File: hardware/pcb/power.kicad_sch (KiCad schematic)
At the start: 53 parts, among them J1 XT30PW-F, J12 Solar, J13 USB-C, U1 AP63205, U11 USBLC6, U12 TP5100, U7 CN3722, U8 MT3608

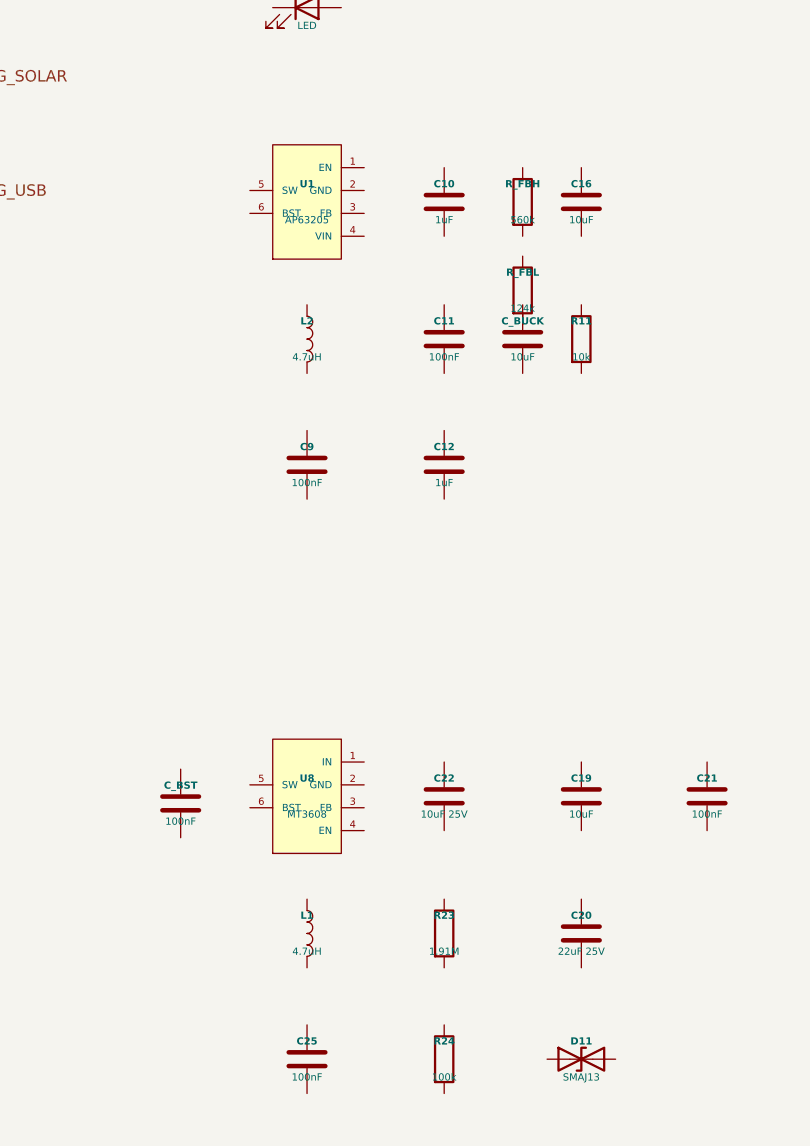
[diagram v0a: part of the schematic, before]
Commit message: hw(pcb): electrical review pass — fix 3V3 regulator variant, boost topology, GPIO13 LED conflict
Full electrical-correctness-gate review of the fresh-start design. Two of
the four CRITICALs from the 2026-05-25 senior review were resolved
incorrectly; this pass corrects them and fixes new findings:

- U1: AP63205WU is the 5 V fixed variant and the R_FBH/R_FBL values
  (560k/124k) assume a 0.6 V reference no AP6320x has — every
  combination overdrives the 3V3 rail. Swap to AP63203WU (3.3 V fixed),
  FB tied to +3V3, R_FBH/R_FBL marked DNP.
- MT3608B VLOOP: documented wiring was a buck topology and the BOM had
  no output rectifier (async boost cannot work without one). Corrected
  to VBAT→L1→SW, added D15 (SS34) and a Q3/Q4 load-disconnect so VBAT
  doesn't leak to the loop terminals through L1+D15 during deep sleep.
- Status LED moved GPIO13 → GPIO14: a green LED + 1k on GPIO13 holds
  the factory-reset strap LOW at boot → NVS wipe every boot. TP13 pad
  added for field factory reset.
- Battery divider reworked to high-side P-FET (Q5): the low-side switch
  left AIN2 biased above ADS1115 VDD through R7 (~14 uA sleep leak).
  C8 100nF → 1nF to fit the firmware's 1 ms enable window.
- TVS D8/D14 SMAJ28CA → SMAJ24CA (zero margin to CN3722 28 V abs max);
  C17 → 35 V/1206; C21 → 50 V; D6 footprint SOD-123 → SMB.
- /CHRG_SOLAR pull-up (R25), VBOOST_EN pull-down (R27), ESP32 EN RC
  (R15/C36) added; C25 duplicate bootstrap cap deleted; C16 assigned as
  U1 VIN bulk.
- schematic_connections.md rewritten pin-name-based with a symbol
  pin-number verification table and datasheet-verification blocker list;
  BOM/placement/guide/placement-script reconciled (phantom refdes,
  wrong ADS1115 pin numbers, mis-documented MPPT divider, shunt return
  path contradiction).

Flagged, not fixed: TP5100 cannot charge 2S from 5 V USB (step-down
charger) — needs an IC swap; schematic still has zero drawn wires; five
IC symbol pinouts pending datasheet verification before ordering.

Co-Auth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
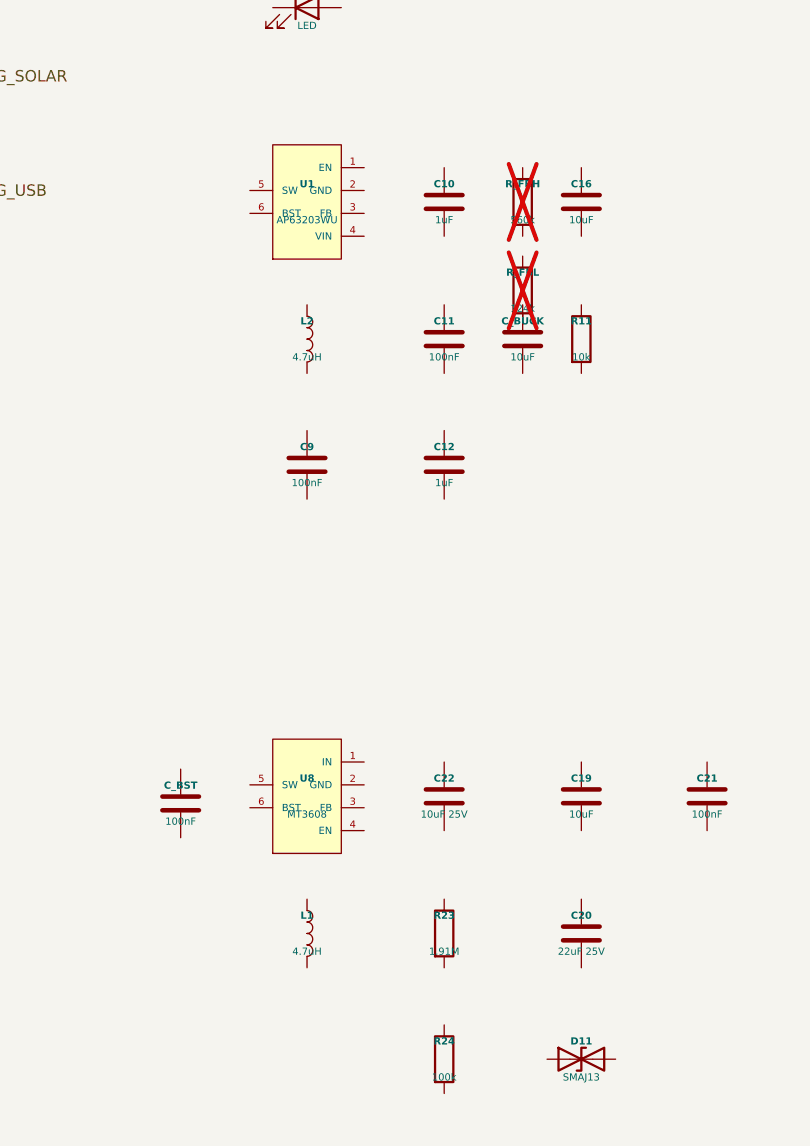
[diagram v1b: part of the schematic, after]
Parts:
- removed C25: 100nF, Capacitor_SMD:C_0402_1005Metric, symbol Device:C
- R_FBH, R_FBL: now not fitted
- U1: value AP63205 -> AP63203WU
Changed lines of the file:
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@@
 	(symbol
 		(lib_id "Device:C")
-		(at 66.04 185.42 0)
-		(unit 1)
-		(body_style 1)
-		(exclude_from_sim no)
-		(in_bom yes)
-		(on_board yes)
-		(in_pos_files yes)
-		(dnp no)
-		(fields_autoplaced yes)
-		(property "Reference" "C25"
-			(at 66.04 183.42 0)
-			(show_name no)
-			(do_not_autoplace no)
-			(effects
-				(font
-					(size 0.8 0.8)
-					(bold yes)
-				)
-			)
-		)
-		(property "Value" "100nF"
-			(at 66.04 187.42 0)
-			(show_name no)
-			(do_not_autoplace no)
-			(effects
-				(font
-					(size 0.8 0.8)
-				)
-			)
-		)
-		(property "Footprint" "Capacitor_SMD:C_0402_1005Metric"
-			(at 0 0 0)
-			(hide yes)
-			(show_name no)
-			(do_not_autoplace no)
-			(effects
-				(font
-					(size 0.8 0.8)
-				)
-			)
-		)
-		(property "Datasheet" ""
-			(at 0 0 0)
-			(hide yes)
-			(show_name no)
-			(do_not_autoplace no)
-			(effects
-				(font
-					(size 0.8 0.8)
-				)
-			)
-		)
-		(property "Description" ""
-			(at 0 0 0)
-			(hide yes)
-			(show_name no)
-			(do_not_autoplace no)
-			(effects
-				(font
-					(size 0.8 0.8)
-				)
-			)
-		)
-		(property "LCSC" "C14663"
-			(at 0 0 0)
-			(hide yes)
-			(show_name no)
-			(do_not_autoplace no)
-			(effects
-				(font
-					(size 0.8 0.8)
-				)
-			)
-		)
-		(pin "1"
-		)
-		(pin "2"
-		)
-		(instances
-			(project "welld"
-				(path "/58c9365f-ec30-52a7-98fc-0e15b15bee29"
-					(reference "C25")
-					(unit 1)
-				)
-				(path "/58c9365f-ec30-52a7-98fc-0e15b15bee29/64fba67a-e021-5c3c-b6fb-14c5c55ee35f/0ab162ba-e49c-5e89-8571-5a4794668fb8"
-					(reference "C25")
-					(unit 1)
-				)
-			)
-		)
-	)
-	(symbol
-		(lib_id "Device:C")
 		(at 185.42 39.37 0)
 		(unit 1)
@@
 			)
 		)
-		(property "Value" "AP63205"
+		(property "Value" "AP63203WU"
 			(at 66.04 92.17 0)
 			(show_name no)
@@
 		(on_board yes)
 		(in_pos_files yes)
-		(dnp no)
+		(dnp yes)
 		(fields_autoplaced yes)
 		(property "Reference" "R_FBH"
@@
 		(on_board yes)
 		(in_pos_files yes)
-		(dnp no)
+		(dnp yes)
 		(fields_autoplaced yes)
 		(property "Reference" "R_FBL"

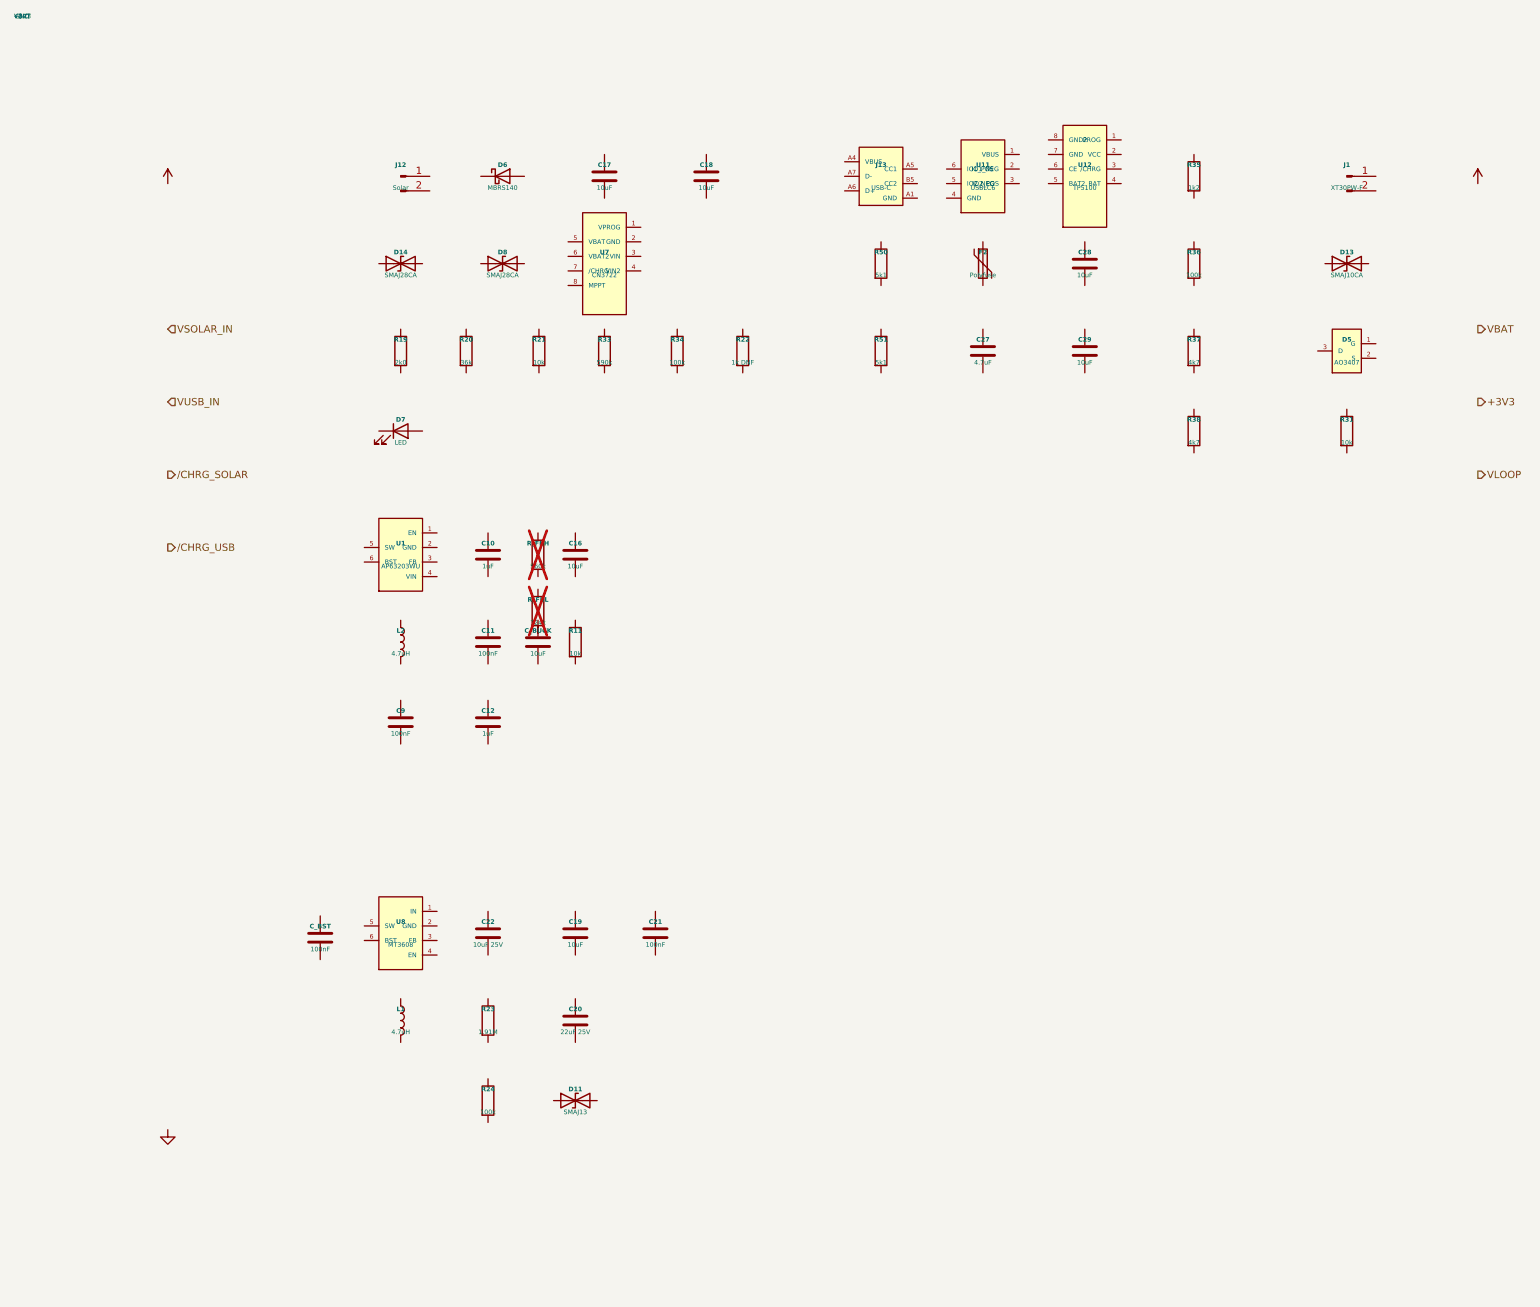
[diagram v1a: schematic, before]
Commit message: hw(pcb): symbol pass — all parts placed, CN3722 redrawn TSSOP-16, CV/MPPT reference bug fixed
Clears the layout gate from senior_review_2026-07-06.md (CRITICALs 1-3)
and fixes a newly found CRITICAL:

- CN3722 CV divider was computed with the CN3791's 1.205 V reference;
  the CN3722's FB reference is 2.416 V (datasheet Rev 1.1, p.4), so the
  documented 590k/100k divider would regulate the 2S pack at ~16.7 V.
  R33 590k -> 243k (8.287 V; formula V_REG = 2.416 x (1 + Rh/Rl) stated
  at every location). Same root cause in the MPPT divider: ref is
  1.04 V, not 1.205 V — old values set the tracking point at 4.8 V,
  below the chip's 7.5 V minimum VCC; R20 36k -> 158k (V_MP ~17.5 V for
  a 12 V-nominal panel, flagged for recompute against the real panel).
- CN3722 symbol redrawn as the real TSSOP-16 (was an 8-pin fiction with
  a nonexistent VPROG pin); full external buck stage placed: M_SOLAR
  P-FET, D16 series + D_SOLAR catch Schottkys, L_SOLAR 47uH, R19
  repurposed as the 0.4R CSP-BAT sense resistor (500 mA), VG cap,
  COM1/2/3 compensation network, RT_SOLAR 10k NTC on TEMP (solar-path
  cold-charge cutoff — review finding O-1 closed for both chargers).
- IP2326 drawn as the verified 24-pin+EPAD part replacing TP5100
  (R36/R37 instances deleted), with R_VSET 120k, RISET 90k, L3 2.2uH,
  RT1 NTC, BST/VSYS caps. Footprint welld:IP2326_TBD pending the LCSC
  package code.
- MT3608B symbol numbering fixed to the standard family map
  (SW=1/GND=2/FB=3/EN=4/IN=5/NC=6; bench-verify note added — datasheet
  fetch was proxy-blocked).
- All previously missing symbols placed: D15, Q3/R29, Q4/R27, Q5/R16,
  R25 (power); R15/C36 EN RC, TP13 (mcu). Values synced: D8/D14
  SMAJ24CA, C8 1nF, C17 35V/1206, F2 2A-hold PTC.
- schematic_connections.md resolution/blocker tables updated; sheets
  still have no drawn wires — the doc remains the wiring authority
  until the wiring pass.

Co-Authored-By: Claude Fable 5 <noreply@anthropic.com>
Claude-Session: https://claude.ai/code/session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
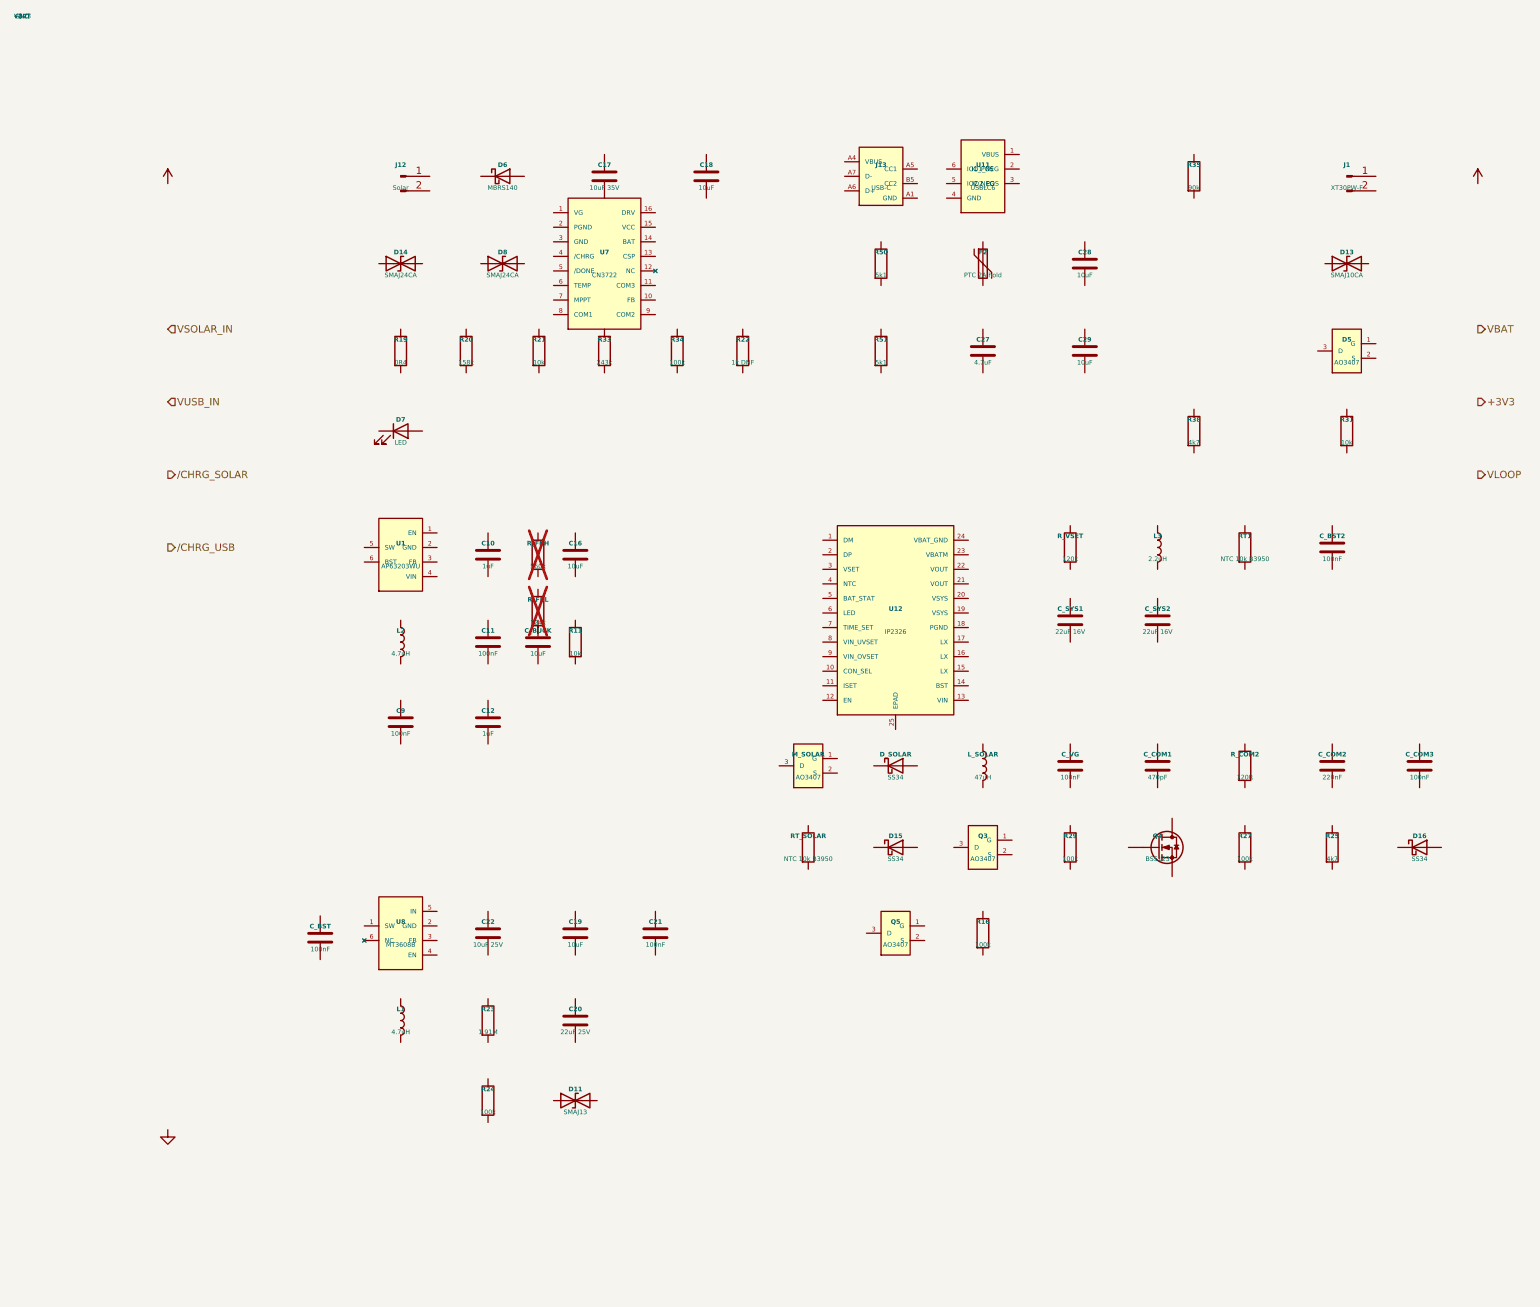
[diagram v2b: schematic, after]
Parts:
- removed R36: 100k, Resistor_SMD:R_0402_1005Metric, symbol Device:R
- removed R37: 4k7, Resistor_SMD:R_0402_1005Metric, symbol Device:R
- removed U12: TP5100, Package_SO:SOIC-8_3.9x4.9mm_P1.27mm, symbol welld:TP5100
- added C_BST2, C_COM3, C_VG: 100nF, Capacitor_SMD:C_0402_1005Metric, symbol Device:C
- added C_COM1: 470pF, Capacitor_SMD:C_0402_1005Metric, symbol Device:C
- added C_COM2: 220nF, Capacitor_SMD:C_0402_1005Metric, symbol Device:C
- added C_SYS1, C_SYS2: 22uF 16V, Capacitor_SMD:C_1206_3216Metric, symbol Device:C
- added D15, D16, D_SOLAR: SS34, Diode_SMD:D_SMA, symbol Device:D_Schottky
- added L3: 2.2uH, Inductor_SMD:L_Bourns-SRN6045TA, symbol Device:L
- added L_SOLAR: 47uH, Inductor_SMD:L_Bourns-SRN6045TA, symbol Device:L
- added M_SOLAR, Q3, Q5: AO3407, Package_TO_SOT_SMD:SOT-23, symbol welld:AO3407
- added Q4: BSS123, Package_TO_SOT_SMD:SOT-23, symbol Device:Q_NMOS
- added R16, R27, R29: 100k, Resistor_SMD:R_0402_1005Metric, symbol Device:R
- added R25: 4k7, Resistor_SMD:R_0402_1005Metric, symbol Device:R
- added RT1, RT_SOLAR: NTC 10k B3950, Resistor_SMD:R_0603_1608Metric, symbol Device:R
- added R_COM2: 120R, Resistor_SMD:R_0402_1005Metric, symbol Device:R
- added R_VSET: 120k, Resistor_SMD:R_0603_1608Metric, symbol Device:R
- added U12: IP2326, welld:IP2326_TBD, symbol welld:IP2326
- C17: value 10uF -> 10uF 35V; footprint Capacitor_SMD:C_0805_2012Metric -> Capacitor_SMD:C_1206_3216Metric
- D14, D8: value SMAJ28CA -> SMAJ24CA
- F2: value Polyfuse -> PTC 2A hold
- R19: value 2k0 -> 0R4; footprint Resistor_SMD:R_0402_1005Metric -> Resistor_SMD:R_1206_3216Metric
- R20: value 36k -> 158k
- R33: value 590k -> 243k
- R35: value 1k2 -> 90k
- U7: footprint Package_SO:SOIC-8_3.9x4.9mm_P1.27mm -> Package_SO:TSSOP-16_4.4x5mm_P0.65mm
- U8: value MT3608 -> MT3608B
